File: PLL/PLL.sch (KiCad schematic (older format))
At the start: 43 parts, among them J1 EuroPower, J2 CV, J3 Gate, J4 Clock, Q1 BC557, Q2 BC547, SW1 Reset, U1 L7805, U2 TL082

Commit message: Starting the PLL
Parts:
- removed C2: 1u, Capacitor_THT:CP_Radial_D8.0mm_P3.80mm, symbol Device:CP
- removed C6: 10n, Capacitor_THT:C_Disc_D7.0mm_W2.5mm_P5.00mm, symbol Device:C
- removed D2, D3, D4, D5: LED, LED_SMD:LED_1206_3216Metric_Castellated, symbol Device:LED
- removed H3, H4: Mounting_Holes, Kosmo_panel:Kosmo_Panel_Dual_Mounting_Holes, symbol Kosmo:Mounting_Holes
- removed Q1: BC557, Package_TO_SOT_THT:TO-92_Inline_Wide, symbol Transistor_BJT:BC557
- removed Q2: BC547, Package_TO_SOT_THT:TO-92_Inline_Wide, symbol Transistor_BJT:BC547
- removed R10, R7, R8, R9: 1k, Resistor_SMD:R_1206_3216Metric_Pad1.42x1.75mm_HandSolder, symbol Device:R
- removed RV1: R_POT_Small, Potentiometer_THT:Potentiometer_Bourns_3339P_Vertical, symbol Device:R_POT_Small
- removed RV3: R_POT_TRIM, Potentiometer_THT:Potentiometer_Bourns_3299W_Vertical, symbol Device:R_POT_TRIM
- removed SW1: Reset, Button_Switch_THT:SW_PUSH_6mm, symbol Switch:SW_SPST
- removed U1: L7805, Package_TO_SOT_THT:TO-220-3_Horizontal_TabDown, symbol Regulator_Linear:L7805
- added C2: 100n, Capacitor_THT:C_Disc_D7.0mm_W2.5mm_P5.00mm, symbol Device:C
- added C6: 10u, Capacitor_THT:CP_Radial_D8.0mm_P3.80mm, symbol Device:CP
- added J10: D8, telec:JackHole, symbol Connector:AudioJack3_Switch
- added J5: M4, telec:JackHole, symbol Connector:AudioJack3_Switch
- added J6: M2, telec:JackHole, symbol Connector:AudioJack3_Switch
- added J7: M1, telec:JackHole, symbol Connector:AudioJack3_Switch
- added J8: D2, telec:JackHole, symbol Connector:AudioJack3_Switch
- added J9: D4, telec:JackHole, symbol Connector:AudioJack3_Switch
- added R13, R14, R15, R16, R17, R18, R19: 100k, Resistor_THT:R_Axial_DIN0204_L3.6mm_D1.6mm_P7.62mm_Horizontal, symbol Device:R
- added R20, R21, R22, R23, R24, R25, R26: 1k, Resistor_THT:R_Axial_DIN0204_L3.6mm_D1.6mm_P7.62mm_Horizontal, symbol Device:R
- added RV1, RV3, RV4, RV5, RV6, RV7: 100k, Potentiometer_THT:Potentiometer_Piher_T-16L_Single_Vertical_Hole, symbol Device:R_POT
- J2: value CV -> Mix
- J3: value Gate -> M8
- LOGO1: footprint logo:telec-32 -> logo:telec-8
- R12, R3: value 10k -> 100k
- R2: value 1k -> 100k
- R5: value 100k -> 470k
- R6: value 10k -> 470k
- RV2: value R_POT -> 100k
- U1: renamed from U?; value 4046 -> CD4046
- U3: renamed from U?; value 4040 -> CD4040
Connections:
- net labels added: Clk_in, Clk_out, D2, D4, D8, IN, M1, M2, M4, M8
- net labels removed: +5V, Rst
- wire segments 51 -> 106
- no-connect marks 11 -> 45
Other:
- note removed: "Output buffer"
- moved on the sheet: D1, J2, J3, J4, R1, RV2, U1, U2B, U3

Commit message: It fits !
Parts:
- added C?: 10u, Capacitor_THT:CP_Radial_D4.0mm_P1.50mm, symbol Device:CP
- added C?: 1u, Capacitor_THT:CP_Radial_D4.0mm_P1.50mm, symbol Device:CP
- added SW1: Freq range, telec:SW_L13.2mm_W7.9mm_P4.7mm, symbol Switch:SW_SPDT_MSM
- C6: footprint Capacitor_THT:CP_Radial_D8.0mm_P3.80mm -> Capacitor_THT:CP_Radial_D4.0mm_P1.50mm
- D1: footprint Diode_THT:D_DO-35_SOD27_P7.62mm_Horizontal -> Diode_SMD:D_1206_3216Metric_Pad1.42x1.75mm_HandSolder
- R1, R19, R2, R3: footprint Resistor_THT:R_Axial_DIN0204_L3.6mm_D1.6mm_P7.62mm_Horizontal -> Resistor_SMD:R_1206_3216Metric_Pad1.42x1.75mm_HandSolder
- U1, U3: footprint (none) -> Package_DIP:DIP-16_W7.62mm_LongPads
- U2: footprint Package_DIP:DIP-8_W7.62mm_LongPads -> Package_SO:SOIC-8_3.9x4.9mm_P1.27mm
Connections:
- net +12V: now also C5.2
- net -12V: no longer C5.2
- net D2: now also U3.6 (Q2); no longer U3.3 (Q4)
- net D4: now also U3.7 (Q1); no longer U3.2 (Q5)
- net D8: now also U3.9 (Q0); no longer U3.4 (Q6)
- net GND: now also C?.2, C?.2
- net M2: now also U3.3 (Q4); no longer U3.6 (Q2)
- net M4: now also U3.2 (Q5); no longer U3.7 (Q1)
- net M8: now also U3.4 (Q6); no longer U3.9 (Q0)
- net at C3.2, R6.2: now also SW1.2
- new net: C?.1, SW1.1
- new net: C?.1, SW1.3
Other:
- moved on the sheet: C3
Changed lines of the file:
@@
 F 0 "U2" H 908 2696 50  0000 L CNN
 F 1 "TL082" H 908 2605 50  0000 L CNN
-F 2 "Package_DIP:DIP-8_W7.62mm_LongPads" H 950 2650 50  0001 C CNN
+F 2 "Package_SO:SOIC-8_3.9x4.9mm_P1.27mm" H 950 2650 50  0001 C CNN
 F 3 "http://www.ti.com/lit/ds/symlink/tl081.pdf" H 950 2650 50  0001 C CNN
 	3    950  2650
@@
 $EndComp
 $Comp
-L power:-12V #PWR016
-U 1 1 60C36318
-P 1800 2500
-F 0 "#PWR016" H 1800 2600 50  0001 C CNN
-F 1 "-12V" H 1815 2673 50  0000 C CNN
-F 2 "" H 1800 2500 50  0001 C CNN
-F 3 "" H 1800 2500 50  0001 C CNN
-	1    1800 2500
-	-1   0    0    -1
-$EndComp
-$Comp
 L Device:LED D6
 U 1 1 60C6FA41
@@
 F 0 "D1" H 3300 4416 50  0000 C CNN
 F 1 "1N4148" H 3300 4325 50  0000 C CNN
-F 2 "Diode_THT:D_DO-35_SOD27_P7.62mm_Horizontal" H 3300 4025 50  0001 C CNN
+F 2 "Diode_SMD:D_1206_3216Metric_Pad1.42x1.75mm_HandSolder" H 3300 4025 50  0001 C CNN
 F 3 "https://assets.nexperia.com/documents/data-sheet/1N4148_1N4448.pdf" H 3300 4200 50  0001 C CNN
 	1    3300 4200
@@
 F 0 "U1" H 5250 3450 50  0000 C CNN
 F 1 "CD4046" H 5300 3350 50  0000 C CNN
-F 2 "" H 5100 2800 50  0001 C CNN
+F 2 "Package_DIP:DIP-16_W7.62mm_LongPads" H 5100 2800 50  0001 C CNN
 F 3 "https://assets.nexperia.com/documents/data-sheet/HEF4046B.pdf" H 5100 2800 50  0001 C CNN
 	1    5100 2800
@@
 F 0 "U3" H 7350 3850 50  0000 C CNN
 F 1 "CD4040" H 7400 3750 50  0000 C CNN
-F 2 "" H 7200 3100 50  0001 C CNN
+F 2 "Package_DIP:DIP-16_W7.62mm_LongPads" H 7200 3100 50  0001 C CNN
 F 3 "http://www.intersil.com/content/dam/Intersil/documents/cd40/cd4020bms-24bms-40bms.pdf" H 7200 3100 50  0001 C CNN
 	1    7200 3100
@@
 F 0 "U2" H 2950 4450 50  0000 C CNN
 F 1 "TL082" H 3000 4350 50  0000 C CNN
-F 2 "Package_DIP:DIP-8_W7.62mm_LongPads" H 2750 4200 50  0001 C CNN
+F 2 "Package_SO:SOIC-8_3.9x4.9mm_P1.27mm" H 2750 4200 50  0001 C CNN
 F 3 "http://www.ti.com/lit/ds/symlink/tl081.pdf" H 2750 4200 50  0001 C CNN
 	1    2750 4200
@@
 F 0 "R3" V 2600 4450 50  0000 L CNN
 F 1 "100k" V 2700 4450 50  0000 L CNN
-F 2 "Resistor_THT:R_Axial_DIN0204_L3.6mm_D1.6mm_P7.62mm_Horizontal" V 2630 4550 50  0001 C CNN
+F 2 "Resistor_SMD:R_1206_3216Metric_Pad1.42x1.75mm_HandSolder" V 2630 4550 50  0001 C CNN
 F 3 "~" H 2700 4550 50  0001 C CNN
 	1    2700 4550
@@
 F 0 "R2" V 2100 4450 50  0000 L CNN
 F 1 "100k" V 2200 4450 50  0000 L CNN
-F 2 "Resistor_THT:R_Axial_DIN0204_L3.6mm_D1.6mm_P7.62mm_Horizontal" V 2130 4550 50  0001 C CNN
+F 2 "Resistor_SMD:R_1206_3216Metric_Pad1.42x1.75mm_HandSolder" V 2130 4550 50  0001 C CNN
 F 3 "~" H 2200 4550 50  0001 C CNN
 	1    2200 4550
@@
 F 0 "U2" H 9600 6117 50  0000 C CNN
 F 1 "TL082" H 9600 6026 50  0000 C CNN
-F 2 "Package_DIP:DIP-8_W7.62mm_LongPads" H 9600 5750 50  0001 C CNN
+F 2 "Package_SO:SOIC-8_3.9x4.9mm_P1.27mm" H 9600 5750 50  0001 C CNN
 F 3 "http://www.ti.com/lit/ds/symlink/tl081.pdf" H 9600 5750 50  0001 C CNN
 	2    9600 5750
@@
 F 0 "R1" V 10200 5650 50  0000 L CNN
 F 1 "1k" V 10300 5700 50  0000 L CNN
-F 2 "Resistor_THT:R_Axial_DIN0204_L3.6mm_D1.6mm_P7.62mm_Horizontal" V 10230 5750 50  0001 C CNN
+F 2 "Resistor_SMD:R_1206_3216Metric_Pad1.42x1.75mm_HandSolder" V 10230 5750 50  0001 C CNN
 F 3 "~" H 10300 5750 50  0001 C CNN
 	1    10300 5750
@@
 Wire Wire Line
 	7900 2600 7700 2600
-Text Label 7900 2600 2    50   ~ 0
-M8
 Wire Wire Line
 	7900 2700 7700 2700
@@
 Wire Wire Line
 	7900 3200 7700 3200
-Text Label 7900 2700 2    50   ~ 0
-M4
-Text Label 7900 2800 2    50   ~ 0
-M2
 Text Label 7900 2900 2    50   ~ 0
 M1
-Text Label 7900 3000 2    50   ~ 0
-D2
-Text Label 7900 3100 2    50   ~ 0
-D4
-Text Label 7900 3200 2    50   ~ 0
-D8
 NoConn ~ 7700 3300
 NoConn ~ 7700 3400
@@
 L power:GND #PWR022
 U 1 1 627447A5
-P 5950 3800
-F 0 "#PWR022" H 5950 3550 50  0001 C CNN
-F 1 "GND" V 5955 3672 50  0000 R CNN
-F 2 "" H 5950 3800 50  0001 C CNN
-F 3 "" H 5950 3800 50  0001 C CNN
-	1    5950 3800
+P 5950 4400
+F 0 "#PWR022" H 5950 4150 50  0001 C CNN
+F 1 "GND" V 5955 4272 50  0000 R CNN
+F 2 "" H 5950 4400 50  0001 C CNN
+F 3 "" H 5950 4400 50  0001 C CNN
+	1    5950 4400
 	1    0    0    -1
 $EndComp
@@
 $EndComp
 Wire Wire Line
-	5950 3800 5950 3700
+	5950 4400 5950 4100
 Wire Wire Line
 	5950 2600 5600 2600
@@
 L Device:C C3
 U 1 1 6274CA19
-P 5950 3550
+P 5950 3950
 AR Path="/6274CA19" Ref="C3"  Part="1"
 AR Path="/5F345A0C/6274CA19" Ref="C?"  Part="1"
-F 0 "C3" V 6100 3550 50  0000 C CNN
-F 1 "100n" V 6200 3550 50  0000 C CNN
-F 2 "Capacitor_THT:C_Disc_D7.0mm_W2.5mm_P5.00mm" H 5988 3400 50  0001 C CNN
-F 3 "~" H 5950 3550 50  0001 C CNN
-	1    5950 3550
+F 0 "C3" V 6100 3950 50  0000 C CNN
+F 1 "100n" V 6200 3950 50  0000 C CNN
+F 2 "Capacitor_THT:C_Disc_D7.0mm_W2.5mm_P5.00mm" H 5988 3800 50  0001 C CNN
+F 3 "~" H 5950 3950 50  0001 C CNN
+	1    5950 3950
 	1    0    0    1
 $EndComp
-Wire Wire Line
-	5950 3400 5950 3300
 $Comp
 L Device:C C2
@@
 F 0 "R19" V 9550 5300 50  0000 L CNN
 F 1 "100k" V 9650 5300 50  0000 L CNN
-F 2 "Resistor_THT:R_Axial_DIN0204_L3.6mm_D1.6mm_P7.62mm_Horizontal" V 9580 5400 50  0001 C CNN
+F 2 "Resistor_SMD:R_1206_3216Metric_Pad1.42x1.75mm_HandSolder" V 9580 5400 50  0001 C CNN
 F 3 "~" H 9650 5400 50  0001 C CNN
 	1    9650 5400
@@
 F 0 "C6" H 9000 5150 50  0000 L CNN
 F 1 "10u" H 8950 5050 50  0000 L CNN
-F 2 "Capacitor_THT:CP_Radial_D8.0mm_P3.80mm" H 9288 4950 50  0001 C CNN
+F 2 "Capacitor_THT:CP_Radial_D4.0mm_P1.50mm" H 9288 4950 50  0001 C CNN
 F 3 "~" H 9250 5100 50  0001 C CNN
 	1    9250 5100
@@
 Wire Wire Line
 	9250 5250 9250 5400
+Text Label 7900 2600 2    50   ~ 0
+D8
+Text Label 7900 3200 2    50   ~ 0
+M8
+Text Label 7900 3000 2    50   ~ 0
+M2
+Text Label 7900 3100 2    50   ~ 0
+M4
+Text Label 7900 2700 2    50   ~ 0
+D4
+Text Label 7900 2800 2    50   ~ 0
+D2
+$Comp
+L power:+12V #PWR0101
+U 1 1 62A783F8
+P 1800 2500
+F 0 "#PWR0101" H 1800 2350 50  0001 C CNN
+F 1 "+12V" H 1815 2673 50  0000 C CNN
+F 2 "" H 1800 2500 50  0001 C CNN
+F 3 "" H 1800 2500 50  0001 C CNN
+	1    1800 2500
+	-1   0    0    -1
+$EndComp
+$Comp
+L Switch:SW_SPDT_MSM SW1
+U 1 1 62A8A9FC
+P 5950 3550
+F 0 "SW1" V 5904 3698 50  0000 L CNN
+F 1 "Freq range" V 5995 3698 50  0000 L CNN
+F 2 "telec:SW_L13.2mm_W7.9mm_P4.7mm" H 5950 3550 50  0001 C CNN
+F 3 "~" H 5950 3550 50  0001 C CNN
+	1    5950 3550
+	0    1    1    0
+$EndComp
+Wire Wire Line
+	5950 3350 5950 3300
+Connection ~ 5950 3350
+Wire Wire Line
+	5950 3800 5950 3350
+$Comp
+L power:GND #PWR016
+U 1 1 62A953FE
+P 5600 4400
+F 0 "#PWR016" H 5600 4150 50  0001 C CNN
+F 1 "GND" V 5605 4272 50  0000 R CNN
+F 2 "" H 5600 4400 50  0001 C CNN
+F 3 "" H 5600 4400 50  0001 C CNN
+	1    5600 4400
+	1    0    0    -1
+$EndComp
+Wire Wire Line
+	5600 4400 5600 4300
+$Comp
+L power:GND #PWR029
+U 1 1 62A98D98
+P 6250 4400
+F 0 "#PWR029" H 6250 4150 50  0001 C CNN
+F 1 "GND" V 6255 4272 50  0000 R CNN
+F 2 "" H 6250 4400 50  0001 C CNN
+F 3 "" H 6250 4400 50  0001 C CNN
+	1    6250 4400
+	1    0    0    -1
+$EndComp
+Wire Wire Line
+	6250 4400 6250 4300
+Wire Wire Line
+	5600 4000 5600 3850
+Wire Wire Line
+	5600 3850 5850 3850
+Wire Wire Line
+	5850 3850 5850 3750
+Wire Wire Line
+	6050 3750 6050 3850
+Wire Wire Line
+	6050 3850 6250 3850
+Wire Wire Line
+	6250 3850 6250 4000
+$Comp
+L Device:CP C?
+U 1 1 62AB5D2C
+P 6250 4150
+F 0 "C?" H 6000 4200 50  0000 L CNN
+F 1 "10u" H 5950 4100 50  0000 L CNN
+F 2 "Capacitor_THT:CP_Radial_D4.0mm_P1.50mm" H 6288 4000 50  0001 C CNN
+F 3 "~" H 6250 4150 50  0001 C CNN
+	1    6250 4150
+	1    0    0    -1
+$EndComp
+$Comp
+L Device:CP C?
+U 1 1 62AB671A
+P 5600 4150
+F 0 "C?" H 5350 4200 50  0000 L CNN
+F 1 "1u" H 5300 4100 50  0000 L CNN
+F 2 "Capacitor_THT:CP_Radial_D4.0mm_P1.50mm" H 5638 4000 50  0001 C CNN
+F 3 "~" H 5600 4150 50  0001 C CNN
+	1    5600 4150
+	1    0    0    -1
+$EndComp
 $EndSCHEMATC

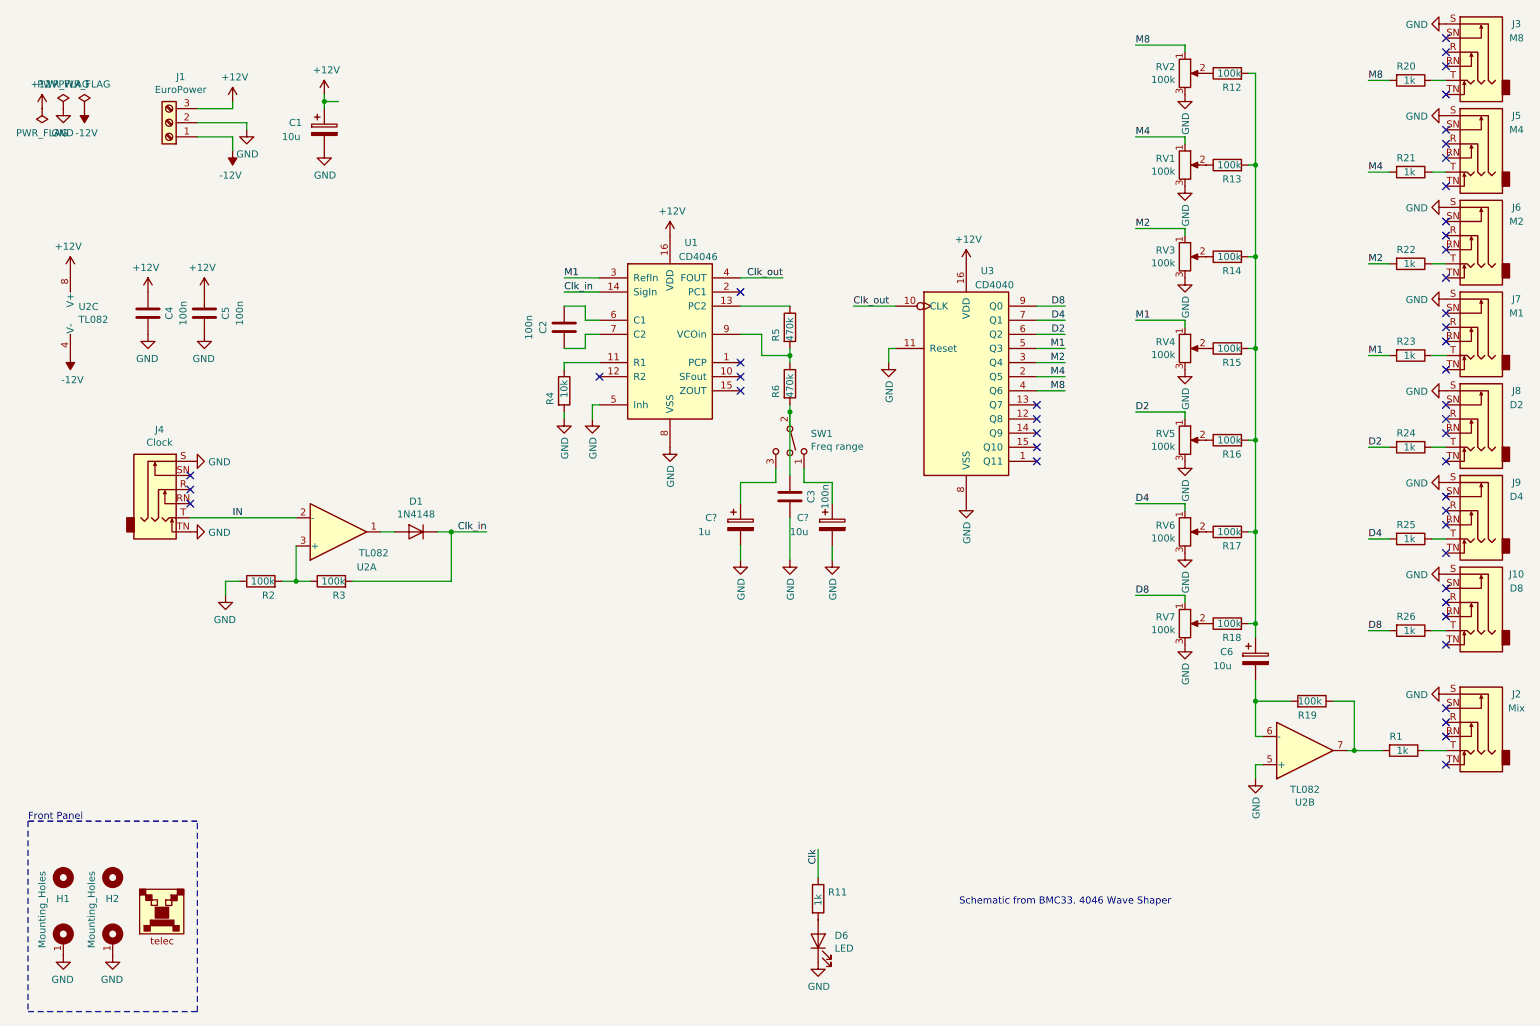
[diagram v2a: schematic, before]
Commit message: PLL layout done
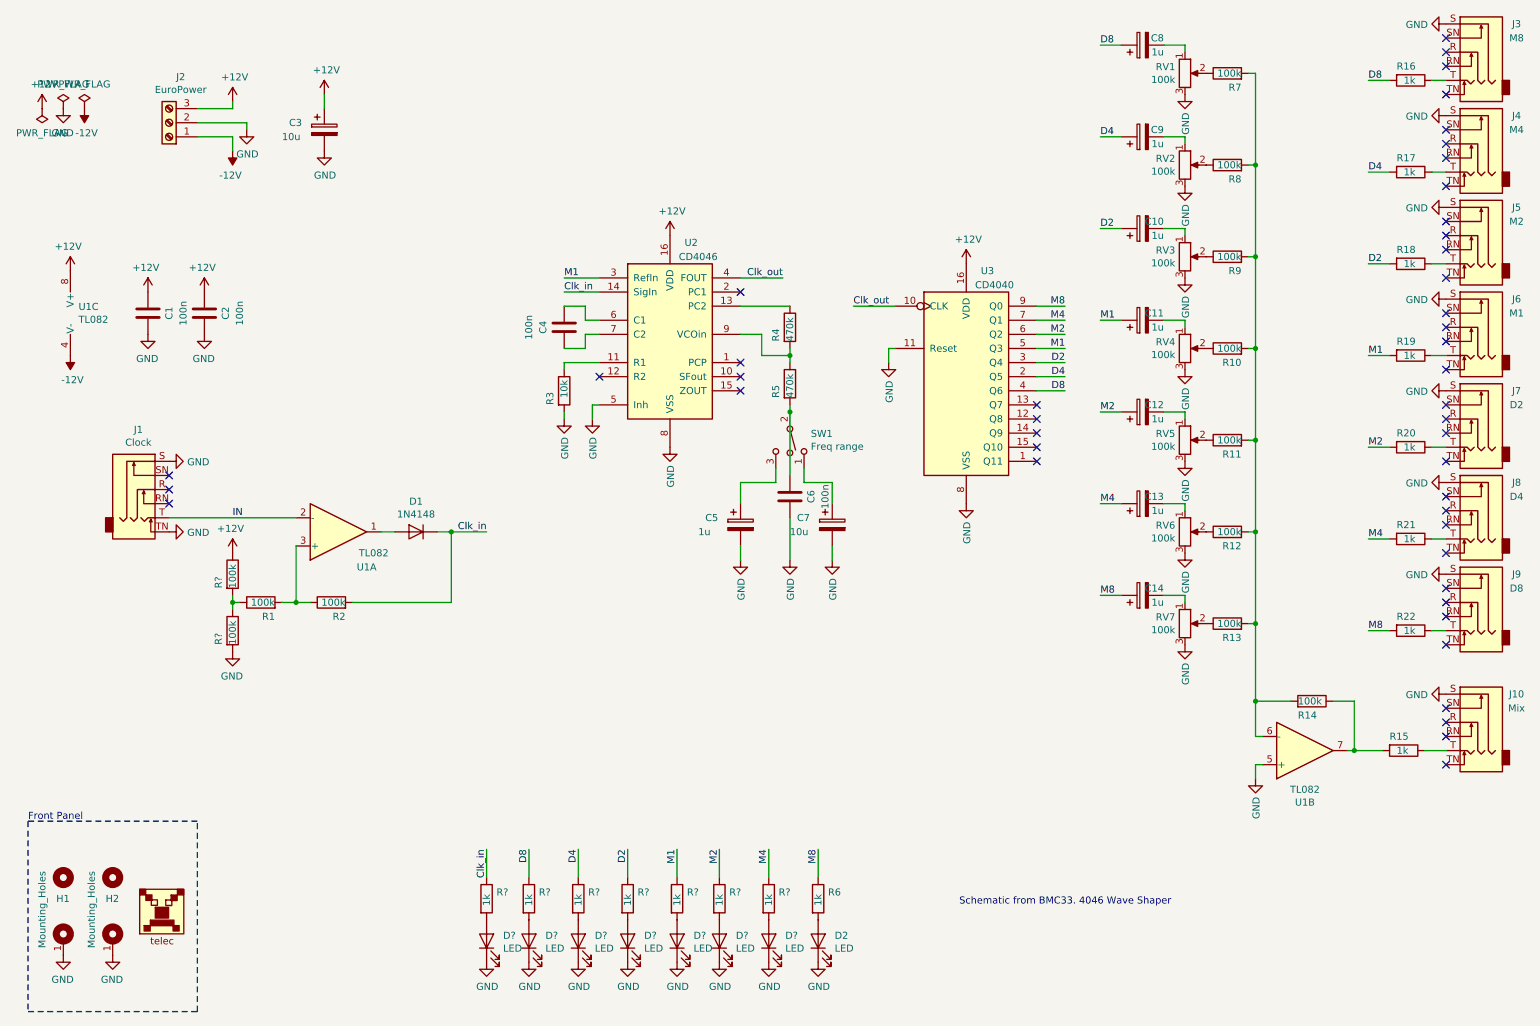
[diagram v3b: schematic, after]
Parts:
- removed C1: 10u, Capacitor_THT:CP_Radial_D8.0mm_P3.80mm, symbol Device:CP
- removed C6: 10u, Capacitor_THT:CP_Radial_D4.0mm_P1.50mm, symbol Device:CP
- added C10, C11, C12, C13, C14, C8, C9: 1u, Capacitor_THT:CP_Radial_D4.0mm_P1.50mm, symbol Device:CP
- added C3: 10u, Capacitor_THT:CP_Radial_D4.0mm_P1.50mm, symbol Device:CP
- added D? (x7): LED, LED_SMD:LED_1206_3216Metric_ReverseMount_Hole1.8x2.4mm, symbol Device:LED
- added R? (x2): 100k, Resistor_SMD:R_1206_3216Metric_Pad1.42x1.75mm_HandSolder, symbol Device:R
- added R? (x7): 1k, Resistor_SMD:R_1206_3216Metric_Pad1.42x1.75mm_HandSolder, symbol Device:R
- gave numbers to parts that had none: 2
- renumbered C4 to C1, C5 to C2, C2 to C4, C3 to C6, D6 to D2, J4 to J1, J2 to J10, J1 to J2, J5 to J4, J6 to J5, J7 to J6, J8 to J7, J9 to J8, J10 to J9, R2 to R1, R15 to R10, R16 to R11, R17 to R12, R18 to R13, R19 to R14, R1 to R15, R20 to R16, R21 to R17, R22 to R18, R23 to R19, R3 to R2, R24 to R20, R25 to R21, R26 to R22, R4 to R3, R5 to R4, R6 to R5, R11 to R6, R12 to R7, R13 to R8, R14 to R9, RV2 to RV1, RV1 to RV2, U2 to U1, U1 to U2
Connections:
- net Clk is gone; now on net M8: R6.1
- net +12V: now also C3.1, R?.1
- net Clk_in: now also R?.1
- net D2: now also R18.2, U3.3 (Q4), C10.1, R?.1; no longer R20.2, RV5.1, U3.6 (Q2)
- net D4: now also R17.2, U3.2 (Q5), C9.1, R?.1; no longer R21.2, RV6.1, U3.7 (Q1)
- net D8: now also R16.2, U3.4 (Q6), C8.1, R?.1; no longer R22.2, RV7.1, U3.9 (Q0)
- net GND: now also C3.2, D?.1 (K), D?.1 (K), D?.1 (K), D?.1 (K), D?.1 (K), D?.1 (K), D?.1 (K), R?.2; no longer R1.1
- net M1: now also C11.1, R?.1; no longer RV4.1
- net M2: now also R20.2, U3.6 (Q2), C12.1, R?.1; no longer R18.2, RV3.1, U3.3 (Q4)
- net M4: now also R21.2, U3.7 (Q1), C13.1, R?.1; no longer R17.2, RV2.1, U3.2 (Q5)
- net M8: now also R22.2, U3.9 (Q0), C14.1; no longer R16.2, RV1.1, U3.4 (Q6)
- net at R14.2, U1.6 (-): now also R10.2, R11.2, R12.2, R13.2, R7.2, R8.2, R9.2
- new net: C8.2, RV1.1
- new net: R1.1, R?.1, R?.2
- new net: C9.2, RV2.1
- new net: C10.2, RV3.1
- new net: C11.2, RV4.1
- new net: C12.2, RV5.1
- new net: C13.2, RV6.1
- new net: C14.2, RV7.1
- new net: D?.2 (A), R?.2 (x7)
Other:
- moved on the sheet: J1, R1, R2
